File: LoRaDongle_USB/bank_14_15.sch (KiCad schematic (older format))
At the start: 8 parts

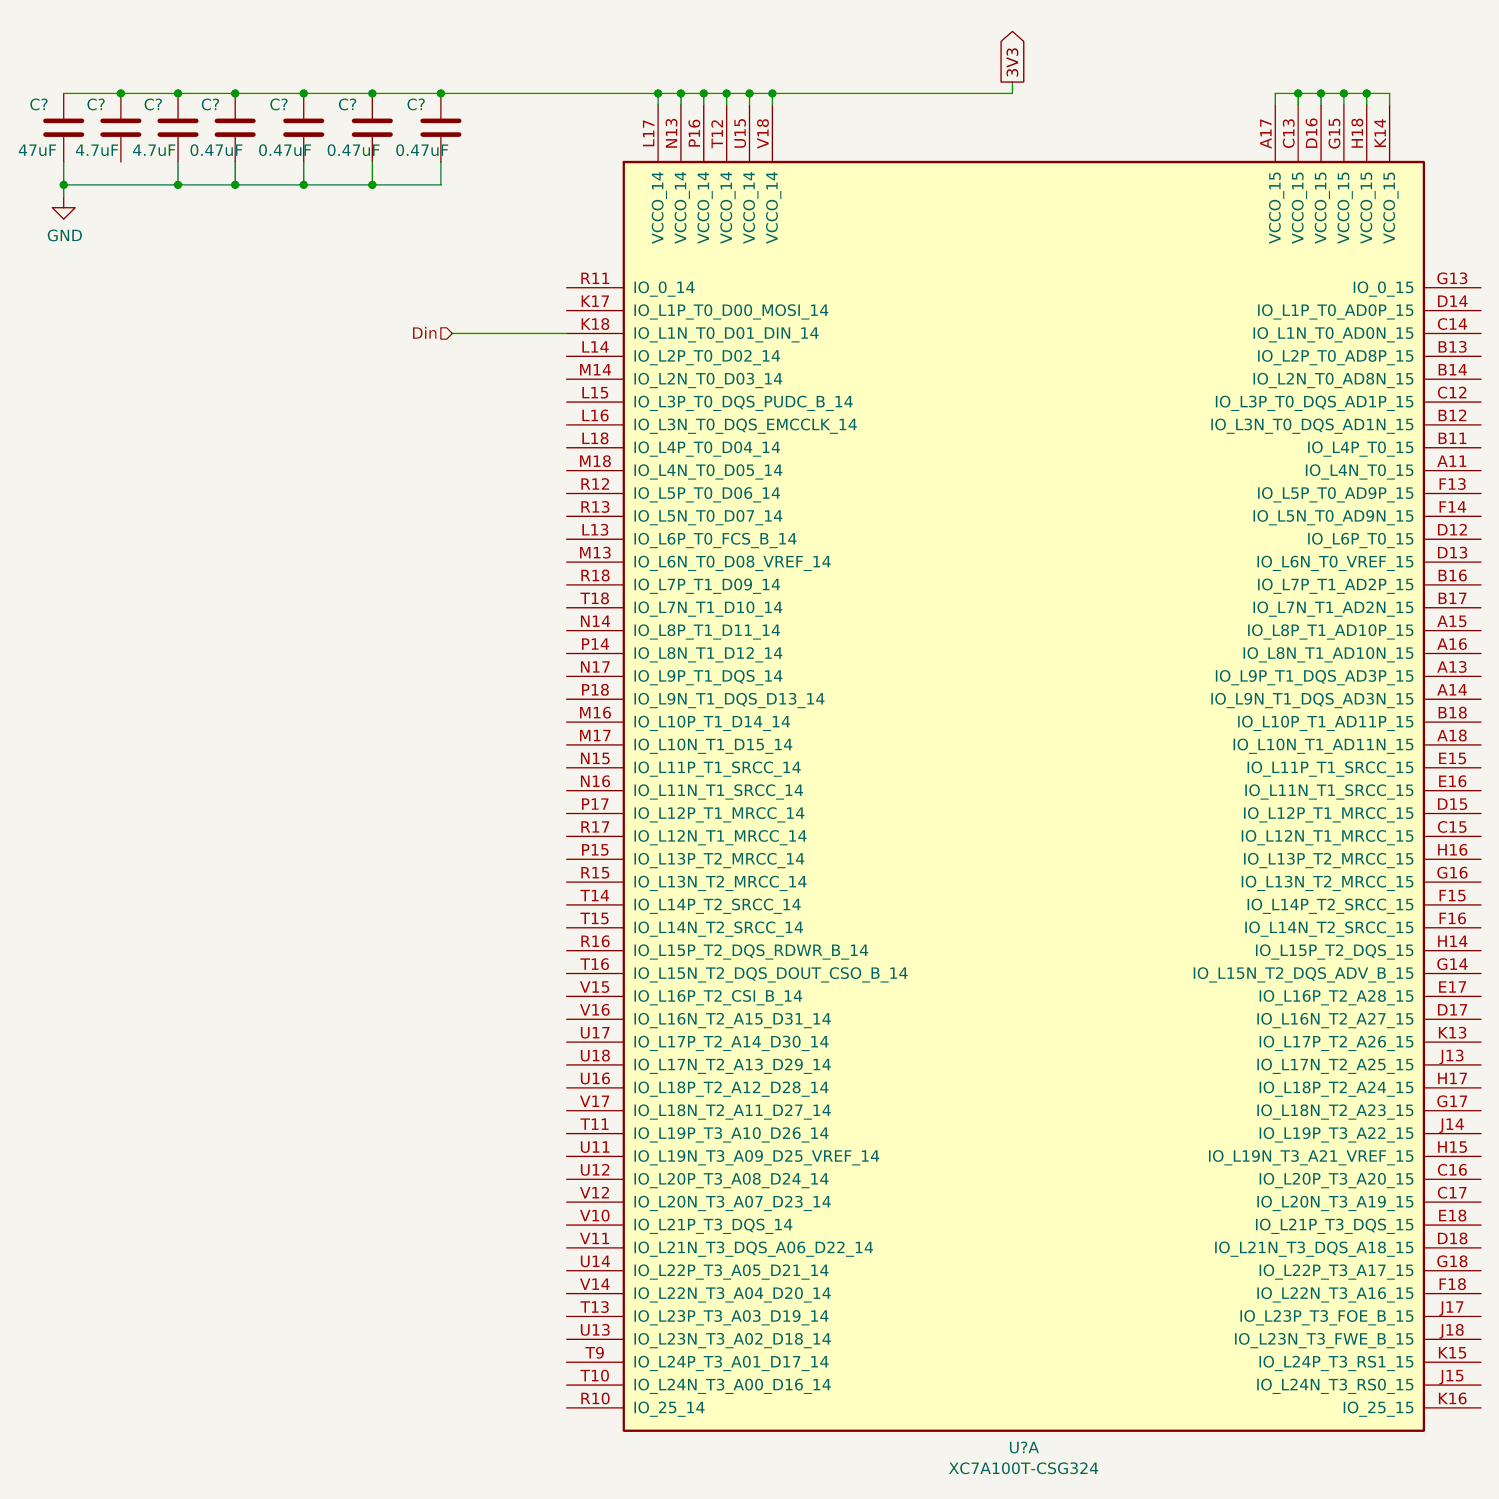
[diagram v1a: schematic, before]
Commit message: added flash memory configuration
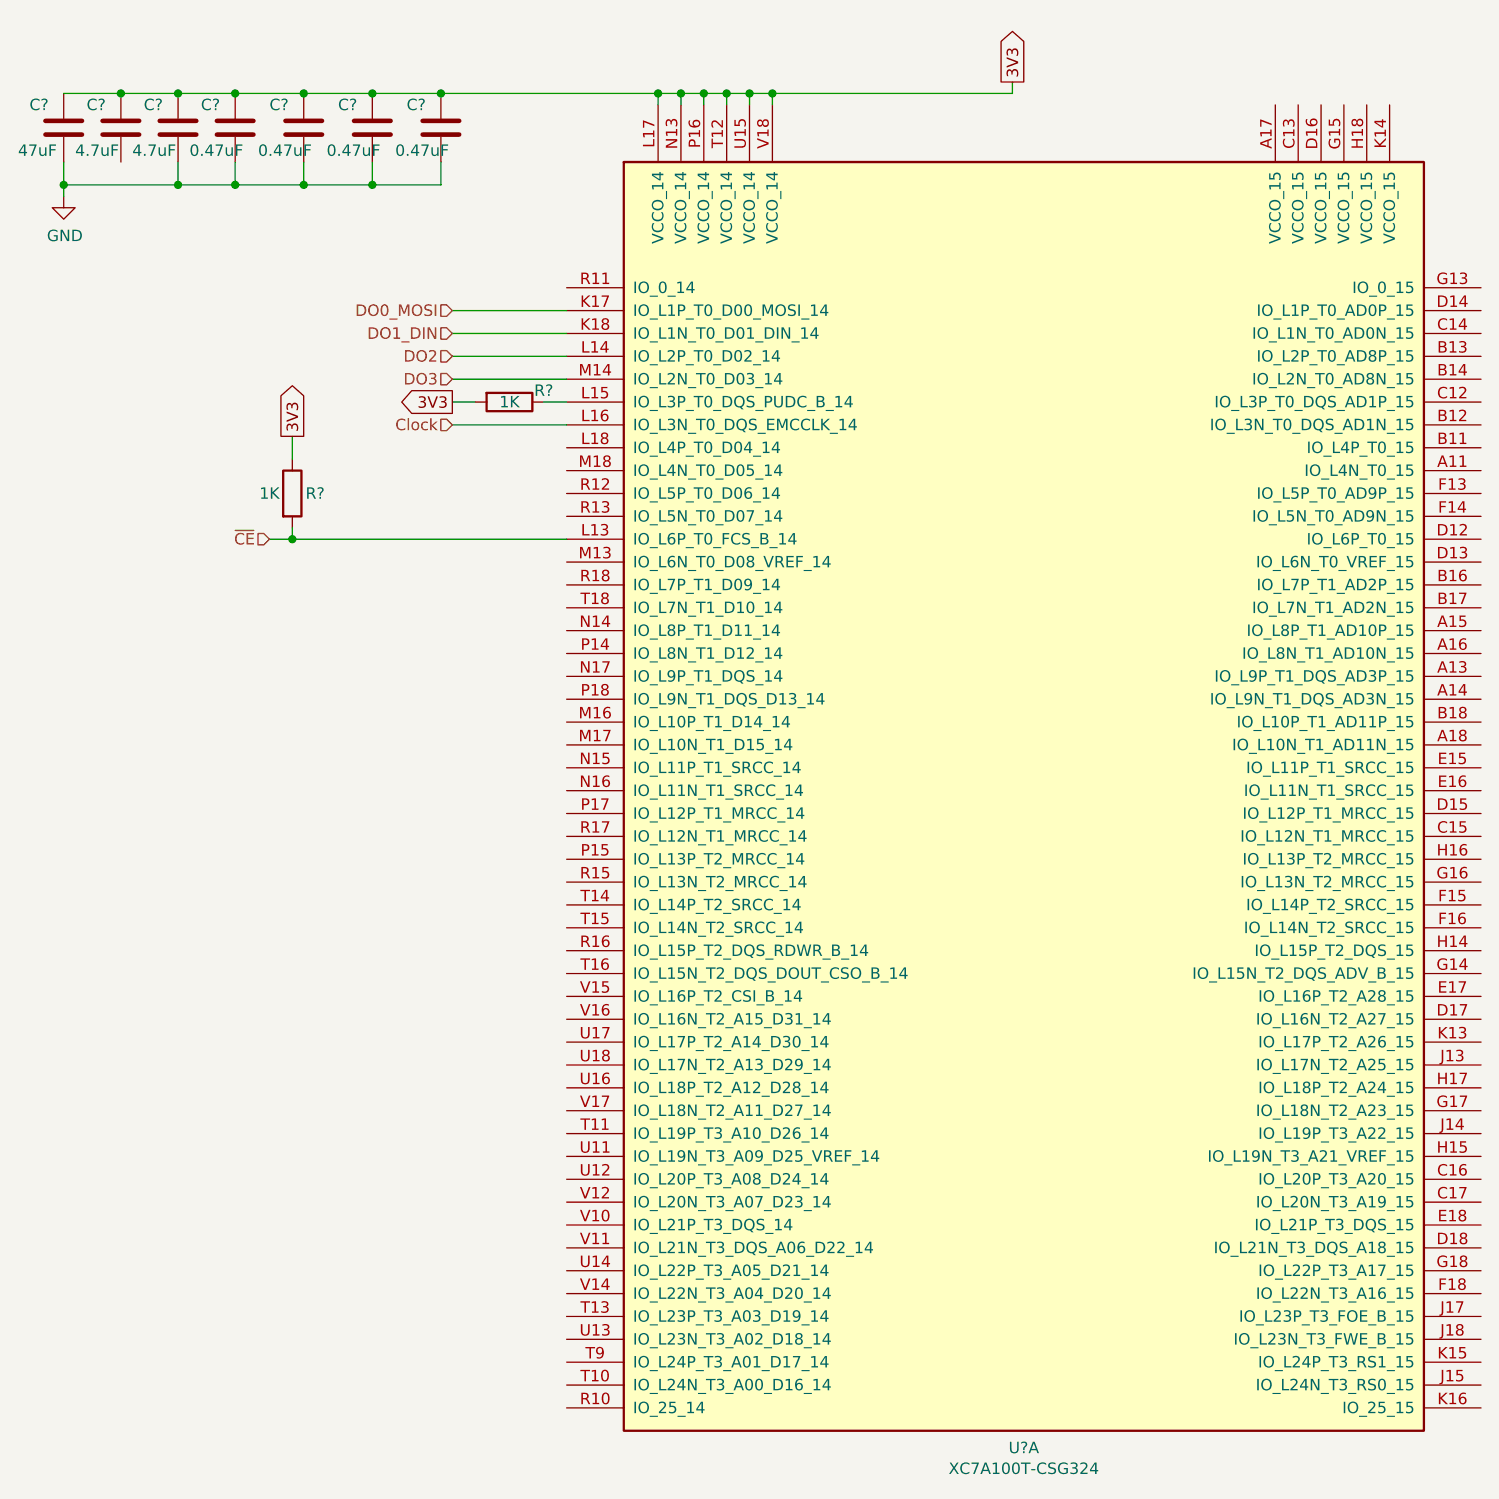
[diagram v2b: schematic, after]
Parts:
- added R? (x2): 1K, Resistor_SMD:R_0402_1005Metric, symbol Device:R
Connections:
- net 3V3: now also R?.1, R?.2
- net DO0_MOSI: now reaches U?.K17 (IO_L1P_T0_D00_MOSI_14)
- net ~CE: now reaches U?.L13 (IO_L6P_T0_FCS_B_14)
- net ~CE: now also R?.2
- net DO2: now reaches U?.L14 (IO_L2P_T0_D02_14)
- net at U?.L15 (IO_L3P_T0_DQS_PUDC_B_14): now also R?.1
- net Clock: now reaches U?.L16 (IO_L3N_T0_DQS_EMCCLK_14)
- net DO3: now reaches U?.M14 (IO_L2N_T0_D03_14)
- net Din renamed DO1_DIN
- now unconnected: U?.A17 (VCCO_15), U?.C13 (VCCO_15), U?.D16 (VCCO_15), U?.G15 (VCCO_15), U?.H18 (VCCO_15), U?.K14 (VCCO_15)
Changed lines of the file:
@@
 	1    0    0    -1
 $EndComp
-Text HLabel 2700 1800 0    50   Input ~ 0
-Din
-Wire Wire Line
-	2700 1800 3200 1800
 Text GLabel 5150 700  1    50   Output ~ 0
 3V3
@@
 Wire Wire Line
 	4000 750  4100 750
-Wire Wire Line
-	6300 800  6300 750
-Wire Wire Line
-	6400 800  6400 750
-Wire Wire Line
-	6400 750  6300 750
-Wire Wire Line
-	6500 800  6500 750
-Wire Wire Line
-	6500 750  6400 750
-Connection ~ 6400 750
-Wire Wire Line
-	6600 800  6600 750
-Wire Wire Line
-	6600 750  6500 750
-Connection ~ 6500 750
-Wire Wire Line
-	6700 800  6700 750
-Wire Wire Line
-	6700 750  6600 750
-Connection ~ 6600 750
-Wire Wire Line
-	6800 800  6800 750
-Wire Wire Line
-	6800 750  6700 750
-Connection ~ 6700 750
 Wire Wire Line
 	3600 750  2650 750
@@
 Wire Wire Line
 	1500 1150 1750 1150
+Wire Wire Line
+	3200 1700 2700 1700
+Text HLabel 2700 1700 0    50   Input ~ 0
+DO0_MOSI
+Wire Wire Line
+	3200 2200 2700 2200
+Text HLabel 2700 2200 0    50   Input ~ 0
+Clock
+$Comp
+L Device:R R?
+U 1 1 6181A6CA
+P 2950 2100
+F 0 "R?" V 2900 2250 50  0000 C CNN
+F 1 "1K" V 2950 2100 50  0000 C CNN
+F 2 "Resistor_SMD:R_0402_1005Metric" V 2880 2100 50  0001 C CNN
+F 3 "~" H 2950 2100 50  0001 C CNN
+F 4 "0402" V 2950 2100 50  0001 C CNN "Physical Size"
+	1    2950 2100
+	0    1    1    0
+$EndComp
+Wire Wire Line
+	3100 2100 3200 2100
+Wire Wire Line
+	2800 2100 2700 2100
+Text GLabel 2700 2100 0    50   Output ~ 0
+3V3
+Wire Wire Line
+	2000 2350 2000 2250
+Text GLabel 2000 2250 1    50   Output ~ 0
+3V3
+$Comp
+L Device:R R?
+U 1 1 6184BE91
+P 2000 2500
+F 0 "R?" H 2100 2500 50  0000 C CNN
+F 1 "1K" H 1900 2500 50  0000 C CNN
+F 2 "Resistor_SMD:R_0402_1005Metric" V 1930 2500 50  0001 C CNN
+F 3 "~" H 2000 2500 50  0001 C CNN
+F 4 "0402" V 2000 2500 50  0001 C CNN "Physical Size"
+	1    2000 2500
+	1    0    0    -1
+$EndComp
+Wire Wire Line
+	2000 2700 2000 2650
+Wire Wire Line
+	2000 2700 1900 2700
+Text HLabel 1900 2700 0    50   Input ~ 0
+~CE
+Connection ~ 2000 2700
+Wire Wire Line
+	3200 1800 2700 1800
+Text HLabel 2700 1800 0    50   Input ~ 0
+DO1_DIN
+Wire Wire Line
+	3200 1900 2700 1900
+Wire Wire Line
+	3200 2000 2700 2000
+Text HLabel 2700 1900 0    50   Input ~ 0
+DO2
+Text HLabel 2700 2000 0    50   Input ~ 0
+DO3
+Wire Wire Line
+	2000 2700 3200 2700
 $EndSCHEMATC
